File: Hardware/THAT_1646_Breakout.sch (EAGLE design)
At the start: 28 parts, among them IC1 THAT1646, J1 1x4, J2 SN, J3 CHASSIS, J4 TN, J5 RN, J6 OUTPUT

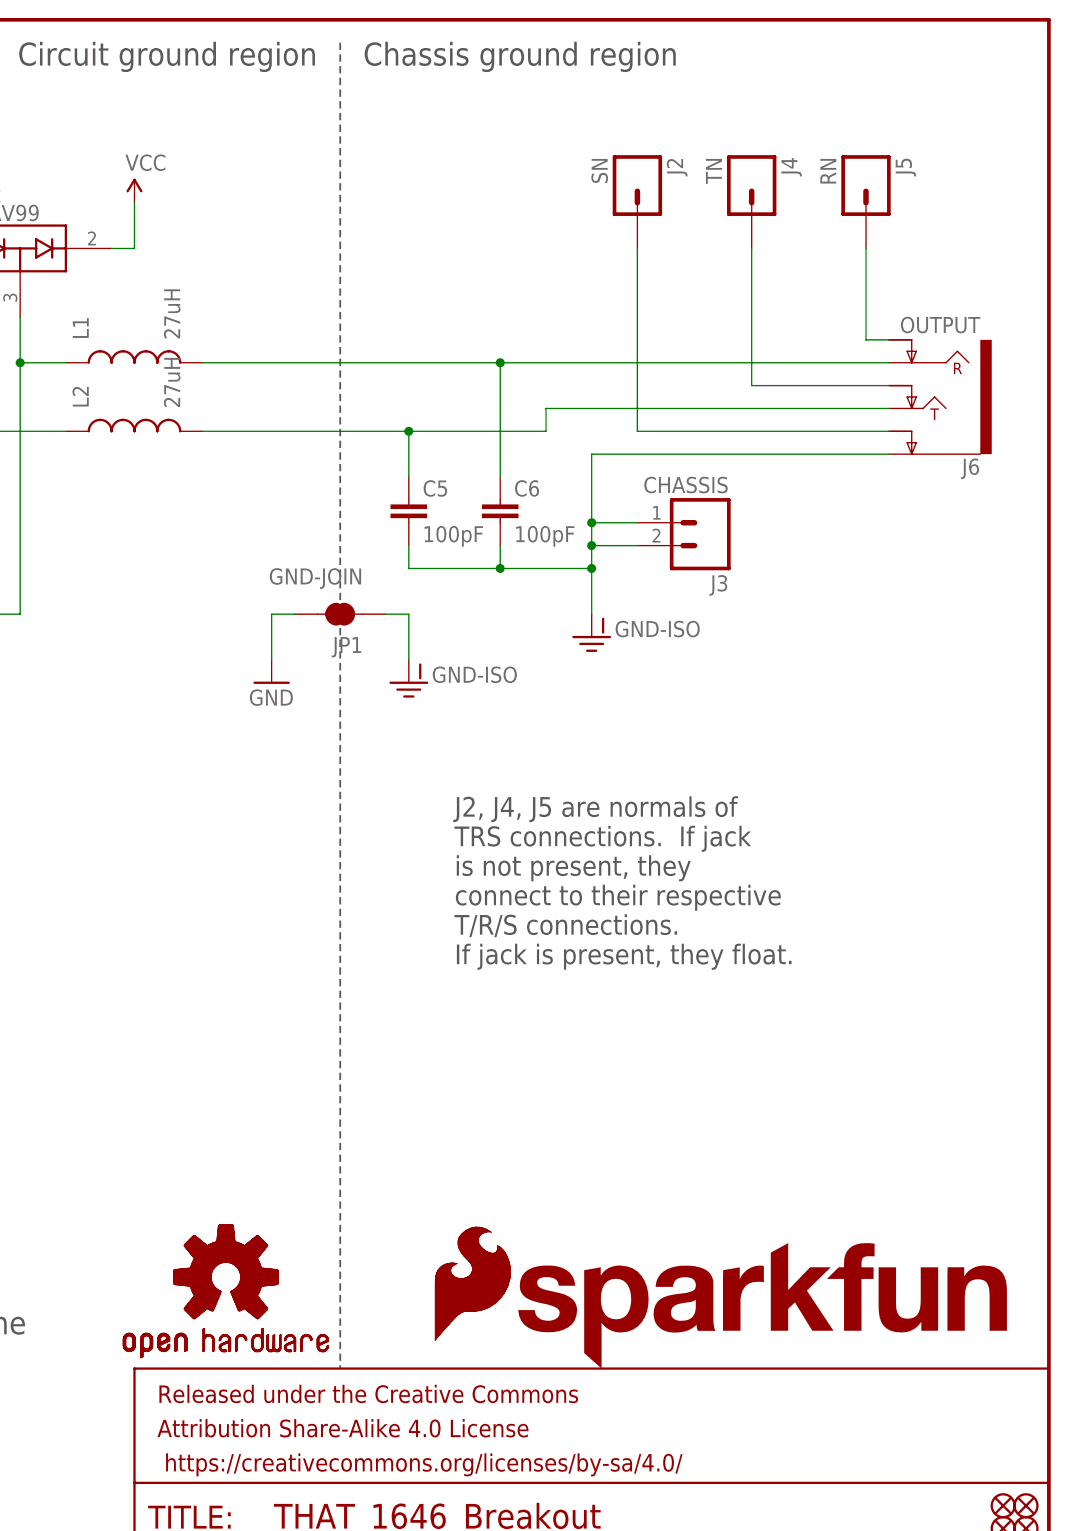
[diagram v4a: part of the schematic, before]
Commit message: Adding testpoints on T/R/S connections.
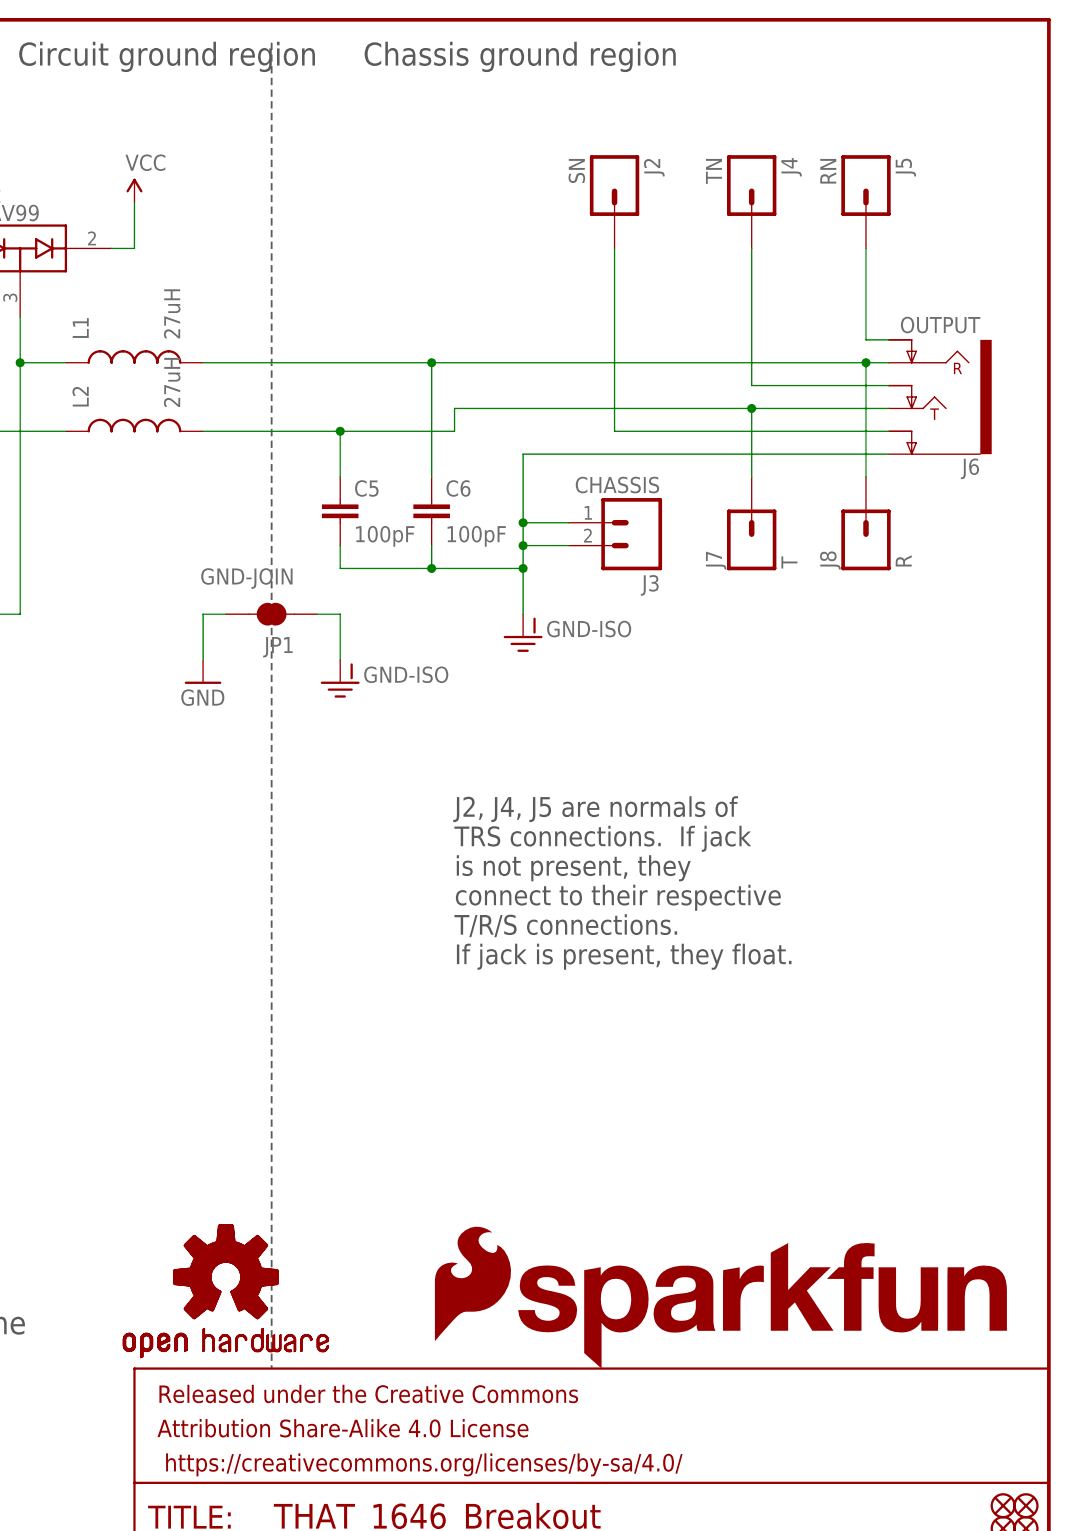
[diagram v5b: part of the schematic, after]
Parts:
- removed LOGO3: SFE_LOGO_FLAME.2_INCH, SparkFun-Aesthetics:SFE_LOGO_FLAME.2_INCH
- added J7: T, SparkFun-Connectors:M01PTH_NO_SILK_YES_STOP
- added J8: R, SparkFun-Connectors:M01PTH_NO_SILK_YES_STOP
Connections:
- net N$8: now also J7.1
- net N$9: now also J8.1
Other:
- moved on the sheet: C5, C6, J2, J3, JP1

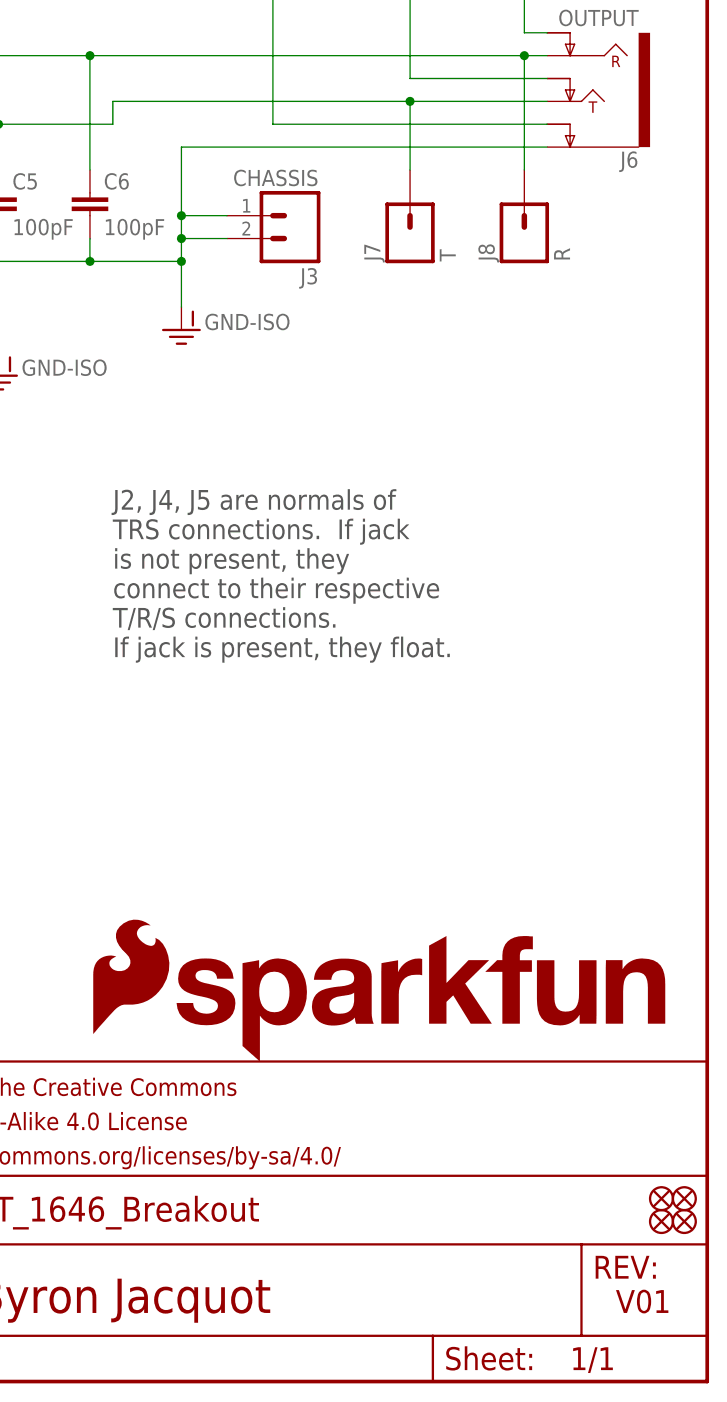
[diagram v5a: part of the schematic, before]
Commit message: Updates after group review.
-Chassis ground pad moved away from selective solder runout.
-Version numbers fixed.
-Top/bottom fiducials co-located.
-Flame oriented to match text.
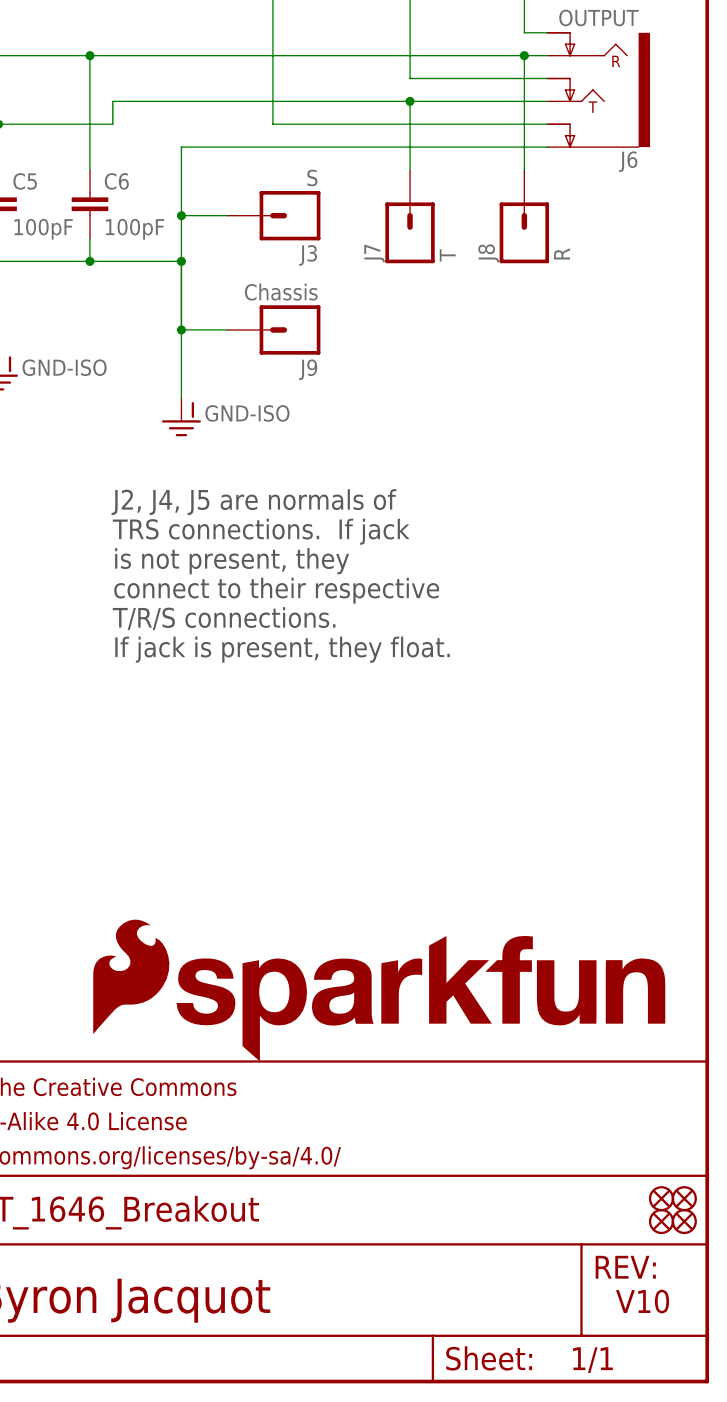
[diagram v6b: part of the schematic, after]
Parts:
- added J9: Chassis, SparkFun-Connectors:M01PTH_NO_SILK_YES_STOP
- J3: value CHASSIS -> S; device SparkFun-Connectors:M021X02_NO_SILK -> SparkFun-Connectors:M01PTH_NO_SILK_YES_STOP
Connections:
- net GND-ISO: now also J9.1; no longer J3.2
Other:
- note added: "V10"
- note removed: "V01"
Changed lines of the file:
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@@
 <part name="SUPPLY2" library="SparkFun-Aesthetics" deviceset="VNEG" device=""/>
 <part name="SUPPLY1" library="SparkFun-Aesthetics" deviceset="VCC" device=""/>
-<part name="J3" library="SparkFun-Connectors" deviceset="M02" device="1X02_NO_SILK" value="CHASSIS"/>
 <part name="FD3" library="SparkFun-Aesthetics" deviceset="FIDUCIAL" device="UFIDUCIAL"/>
 <part name="FD4" library="SparkFun-Aesthetics" deviceset="FIDUCIAL" device="UFIDUCIAL"/>
@@
 <part name="J7" library="SparkFun-Connectors" deviceset="M01" device="PTH_NO_SILK_YES_STOP" value="T"/>
 <part name="J8" library="SparkFun-Connectors" deviceset="M01" device="PTH_NO_SILK_YES_STOP" value="R"/>
+<part name="J9" library="SparkFun-Connectors" deviceset="M01" device="PTH_NO_SILK_YES_STOP" value="Chassis"/>
+<part name="J3" library="SparkFun-Connectors" deviceset="M01" device="PTH_NO_SILK_YES_STOP" value="S"/>
 </parts>
 <sheets>
@@
 <plain>
 <text x="167.64" y="7.62" size="3.81" layer="94" font="vector">Byron Jacquot</text>
-<text x="238.76" y="7.62" size="2.54" layer="94" font="vector">V01</text>
+<text x="238.76" y="7.62" size="2.54" layer="94" font="vector">V10</text>
 <wire x1="162.56" y1="182.88" x2="162.56" y2="35.56" width="0.2032" layer="97" style="longdash"/>
 <text x="172.72" y="180.34" size="2.54" layer="97" font="vector" rot="R180" align="top-right">Chassis ground region</text>
@@
 <instance part="J6" gate="G$1" x="236.22" y="144.78" rot="R180"/>
 <instance part="SUPPLY3" gate="G$1" x="78.74" y="149.86"/>
-<instance part="GND-ISO2" gate="G$1" x="190.5" y="116.84"/>
+<instance part="GND-ISO2" gate="G$1" x="190.5" y="106.68"/>
 <instance part="SUPPLY4" gate="G$2" x="78.74" y="88.9"/>
 <instance part="IC1" gate="G$1" x="71.12" y="111.76"/>
@@
 <instance part="SUPPLY2" gate="G$2" x="48.26" y="106.68"/>
 <instance part="SUPPLY1" gate="G$1" x="43.18" y="129.54"/>
-<instance part="J3" gate="G$1" x="203.2" y="129.54" rot="R180"/>
 <instance part="FD3" gate="G$1" x="246.38" y="20.32"/>
 <instance part="FD4" gate="G$1" x="246.38" y="17.78"/>
@@
 <instance part="J7" gate="G$1" x="215.9" y="127" rot="R90"/>
 <instance part="J8" gate="G$1" x="228.6" y="127" rot="R90"/>
+<instance part="J9" gate="G$1" x="203.2" y="116.84" rot="R180"/>
+<instance part="J3" gate="G$1" x="203.2" y="129.54" rot="R180"/>
 </instances>
 <busses>
@@
 <segment>
 <pinref part="GND-ISO2" gate="G$1" pin="GND-ISO"/>
-<wire x1="190.5" y1="119.38" x2="190.5" y2="124.46" width="0.1524" layer="91"/>
+<wire x1="190.5" y1="109.22" x2="190.5" y2="116.84" width="0.1524" layer="91"/>
 <pinref part="J6" gate="G$1" pin="EARTH"/>
-<wire x1="190.5" y1="124.46" x2="190.5" y2="127" width="0.1524" layer="91"/>
-<wire x1="190.5" y1="127" x2="190.5" y2="129.54" width="0.1524" layer="91"/>
+<wire x1="190.5" y1="124.46" x2="190.5" y2="116.84" width="0.1524" layer="91"/>
+<wire x1="190.5" y1="116.84" x2="190.5" y2="129.54" width="0.1524" layer="91"/>
 <wire x1="190.5" y1="129.54" x2="190.5" y2="137.16" width="0.1524" layer="91"/>
 <wire x1="190.5" y1="137.16" x2="231.14" y2="137.16" width="0.1524" layer="91"/>
@@
 <wire x1="180.34" y1="127" x2="180.34" y2="124.46" width="0.1524" layer="91"/>
 <junction x="180.34" y="124.46"/>
-<pinref part="J3" gate="G$1" pin="1"/>
 <wire x1="195.58" y1="129.54" x2="190.5" y2="129.54" width="0.1524" layer="91"/>
-<pinref part="J3" gate="G$1" pin="2"/>
-<wire x1="190.5" y1="127" x2="195.58" y2="127" width="0.1524" layer="91"/>
-<junction x="190.5" y="127"/>
+<wire x1="190.5" y1="116.84" x2="195.58" y2="116.84" width="0.1524" layer="91"/>
+<junction x="190.5" y="116.84"/>
 <junction x="190.5" y="129.54"/>
 <junction x="190.5" y="124.46"/>
-</segment>
-<segment>
+<pinref part="J9" gate="G$1" pin="1"/>
+<pinref part="J3" gate="G$1" pin="1"/>
+</segment>
+<segment>
